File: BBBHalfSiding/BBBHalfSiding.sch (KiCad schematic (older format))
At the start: 9 parts, among them P8 BeagleBone_Black_Header, P9 BeagleBone_Black_Header, T4 Motor 0, T5 Motor 1, U4 TC4428, U5 TC4428, U6 74HC00

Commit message: Completed Beagle Bone Black Half Siding Cape
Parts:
- added C17: .1 uf, ~, symbol C
- added P11: addr / we, ~, symbol CONN_3X2
- added R10, R11: 5.6K Ohms, ~, symbol R
- added R12, R13, R14: 4.75K Ohms, ~, symbol R
- added R15: 10K Ohms, ~, symbol R
- added U13: CAT24C256W, symbol CAT24C256W
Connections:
- net labels removed: GNDD
- wire segments 109 -> 131

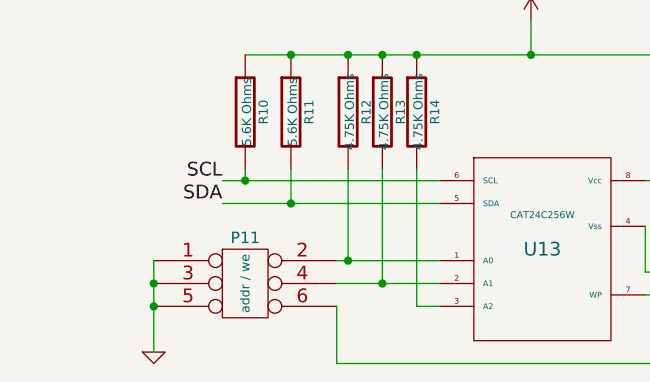
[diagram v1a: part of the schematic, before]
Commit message: Updates to BBBHalfSiding (silk screen tweaks)
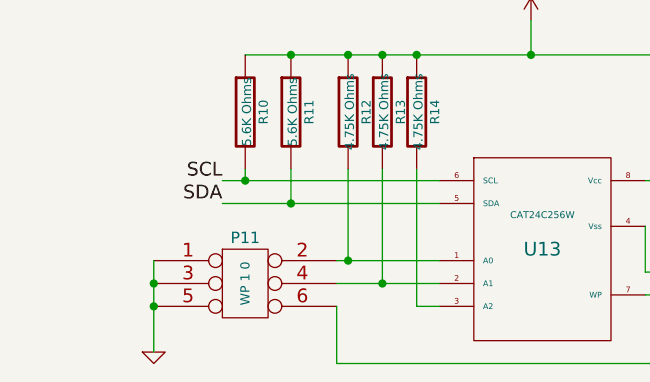
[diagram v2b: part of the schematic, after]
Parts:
- P11: value addr / we -> WP 1 0
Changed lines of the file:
@@
 Sheet 1 4
 Title ""
-Date "19 oct 2018"
+Date "20 oct 2018"
 Rev ""
 Comp ""
@@
 P 1100 7400
 F 0 "P11" H 1100 7650 50  0000 C CNN
-F 1 "addr / we" V 1100 7450 40  0000 C CNN
+F 1 "WP 1 0" V 1100 7450 40  0000 C CNN
 F 2 "~" H 1100 7400 60  0000 C CNN
 F 3 "~" H 1100 7400 60  0000 C CNN

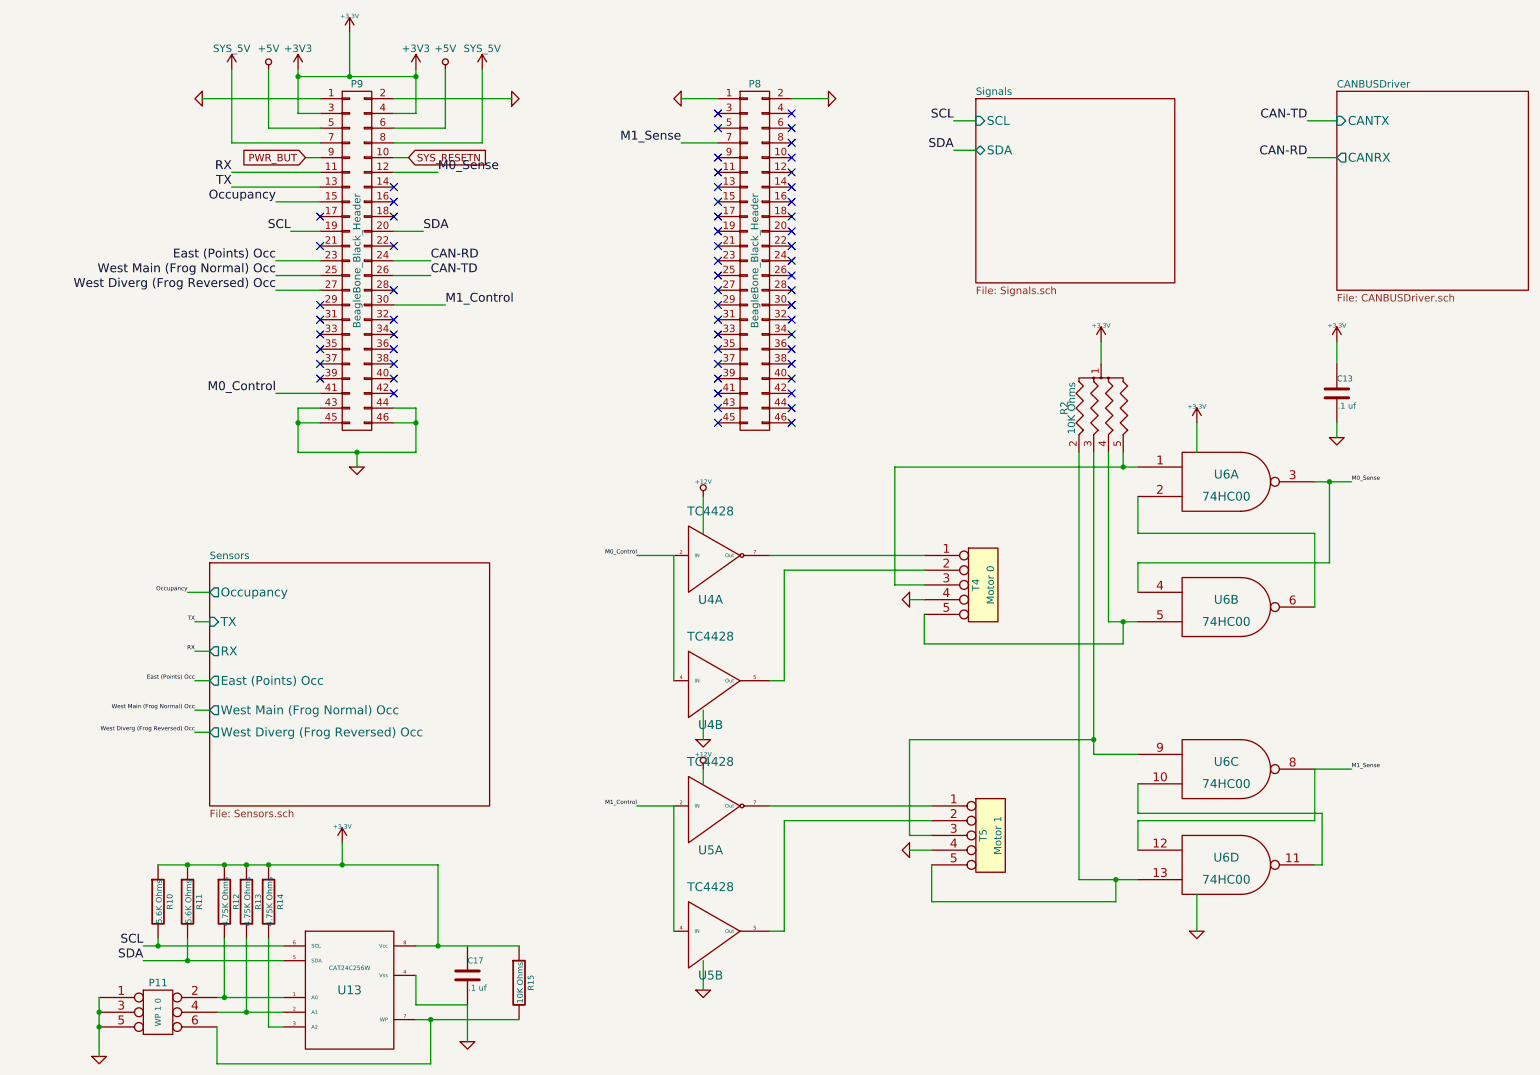
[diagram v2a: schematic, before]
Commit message: Tweaks to map to valid (unused) GPIO pins.
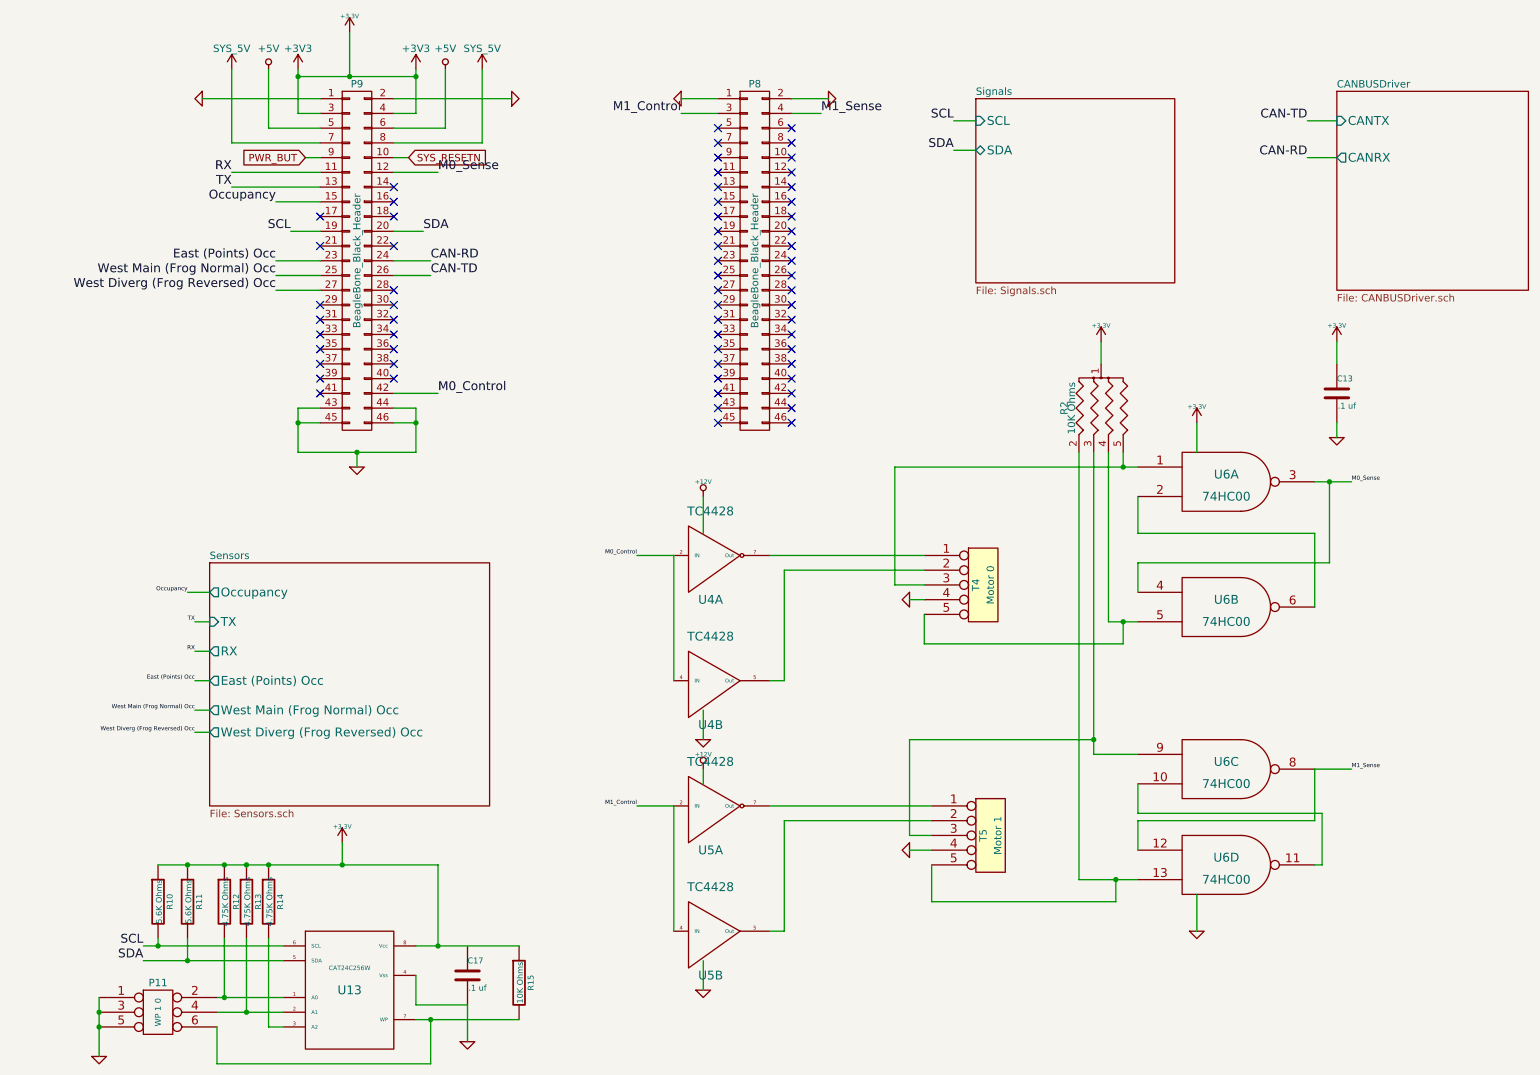
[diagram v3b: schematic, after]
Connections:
- net M0_Control: now also P9.42 (P42); no longer P9.41 (P41)
- net M1_Control: now also P8.3 (P3); no longer P9.30 (P30)
- net M1_Sense: now also P8.4 (P4); no longer P8.7 (P7)
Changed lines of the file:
@@
 Text Label 1900 2450 2    60   ~ 0
 West Diverg (Frog Reversed) Occ
-Text Label 1900 3150 2    60   ~ 0
+Text Label 3000 3150 0    60   ~ 0
 M0_Control
 NoConn ~ 2700 1750
@@
 NoConn ~ 2700 2950
 NoConn ~ 2700 3050
-NoConn ~ 2700 3150
-Text Label 3050 2550 0    60   ~ 0
+Text Label 4650 1250 2    60   ~ 0
 M1_Control
 Text Label 3000 1650 0    60   ~ 0
 M0_Sense
-NoConn ~ 4900 1250
-NoConn ~ 4900 1350
 NoConn ~ 4900 1550
 NoConn ~ 4900 1650
@@
 NoConn ~ 5400 1650
 NoConn ~ 5400 1550
-NoConn ~ 5400 1450
-NoConn ~ 5400 1350
-NoConn ~ 5400 1250
 NoConn ~ 5400 3350
 NoConn ~ 5400 3250
@@
 NoConn ~ 4900 3250
 NoConn ~ 4900 3350
-Text Label 4650 1450 2    60   ~ 0
+Text Label 5600 1250 0    60   ~ 0
 M1_Sense
 $Comp
@@
 	7550 4700 7750 4700
 Wire Wire Line
-	7750 5600 7450 5600
-Wire Wire Line
-	7450 5600 7450 3550
+	7450 5600 7750 5600
+Wire Wire Line
+	7450 3550 7450 5600
 Wire Wire Line
 	7350 3550 7350 6450
@@
 Connection ~ 2450 3550
 Wire Wire Line
-	2700 1250 2850 1250
-Wire Wire Line
-	2850 1250 2850 950
+	2850 1250 2700 1250
+Wire Wire Line
+	2850 950  2850 1250
 Wire Wire Line
 	2700 1350 3050 1350
@@
 	3300 1450 2700 1450
 Wire Wire Line
-	2200 1250 2050 1250
-Wire Wire Line
-	2050 1250 2050 950
+	2050 1250 2200 1250
+Wire Wire Line
+	2050 950  2050 1250
 Wire Wire Line
 	2200 1350 1850 1350
@@
 	1900 2450 2200 2450
 Wire Wire Line
-	1900 3150 2200 3150
-Wire Wire Line
 	3000 1650 2700 1650
-Wire Wire Line
-	3050 2550 2700 2550
-Wire Wire Line
-	4650 1450 4900 1450
 Wire Wire Line
 	1000 6900 1950 6900
@@
 	0    1    1    0
 $EndComp
+Wire Wire Line
+	3000 3150 2700 3150
+NoConn ~ 2200 3150
+NoConn ~ 2700 2550
+Wire Wire Line
+	4650 1250 4900 1250
+Wire Wire Line
+	5600 1250 5400 1250
+NoConn ~ 4900 1350
+NoConn ~ 4900 1450
+NoConn ~ 5400 1350
+NoConn ~ 5400 1450
 $EndSCHEMATC
